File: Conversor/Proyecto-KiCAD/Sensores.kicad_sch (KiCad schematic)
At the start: 28 parts, among them U10 OPA365xxD, U7 TMCS1100A4, U8 LM5056APMH/NOPB, U9 ISO7242C

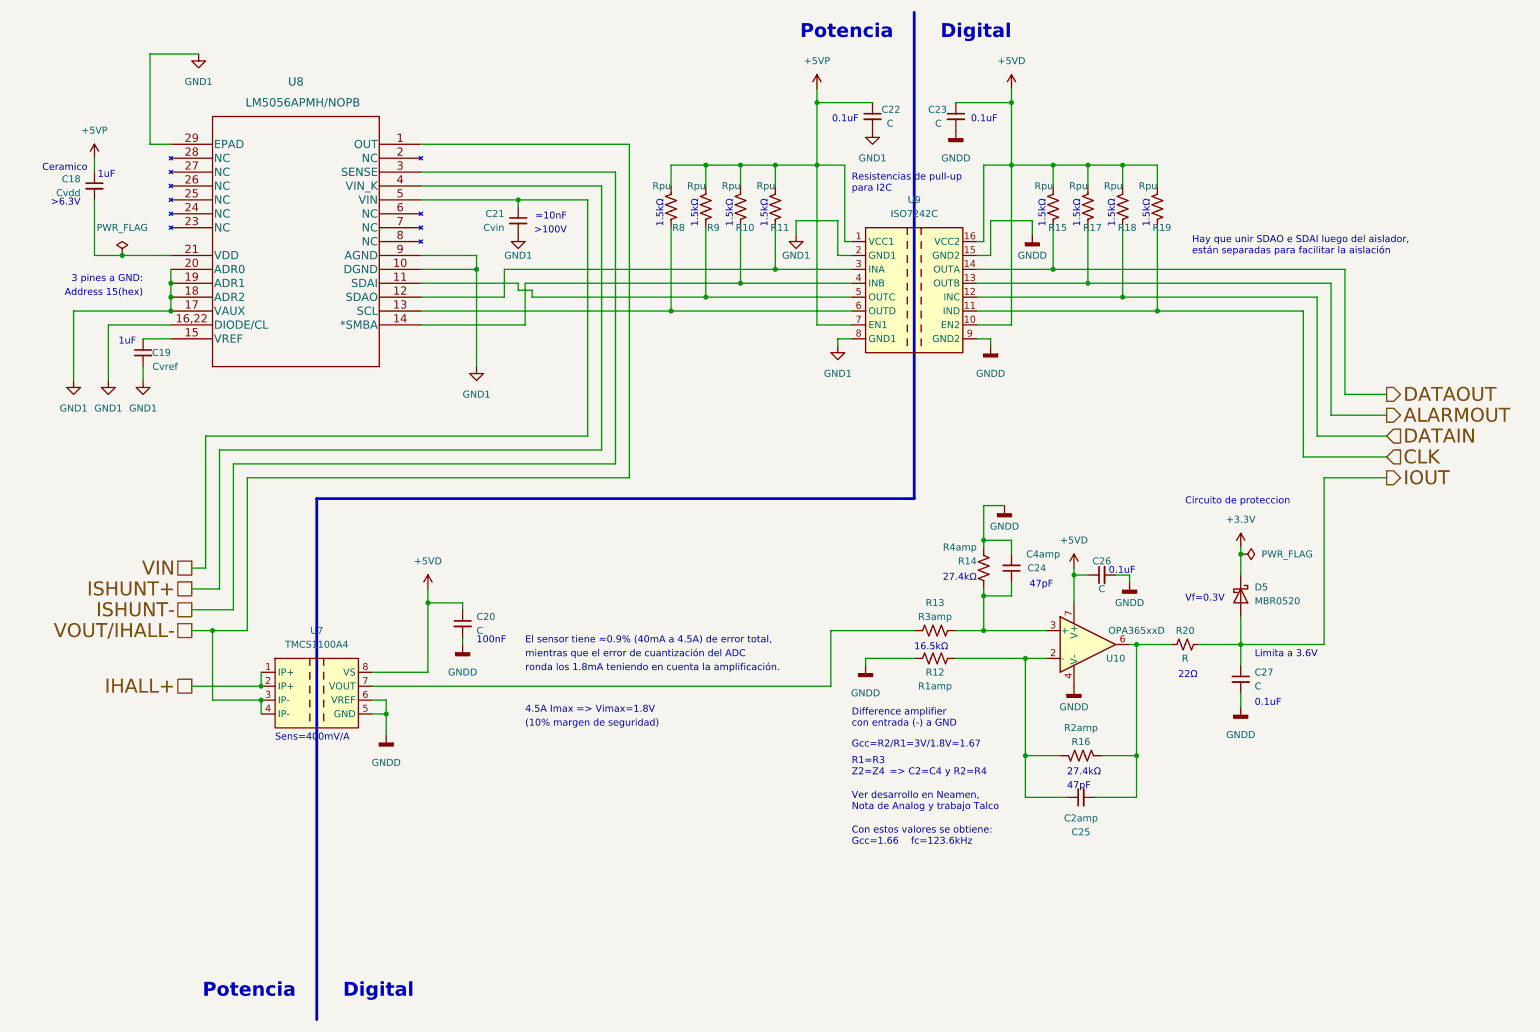
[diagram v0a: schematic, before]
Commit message: Unir las lineas de SDAI y SDAO a la salida del ISO7242C
- Espejar el esquemático en la hoja de sensores, para que sea consistente la separación de Digital/Potencia
Por hacer:

  - Verificar si es correcta la forma de conectar las lineas de datos a la salida del aislador
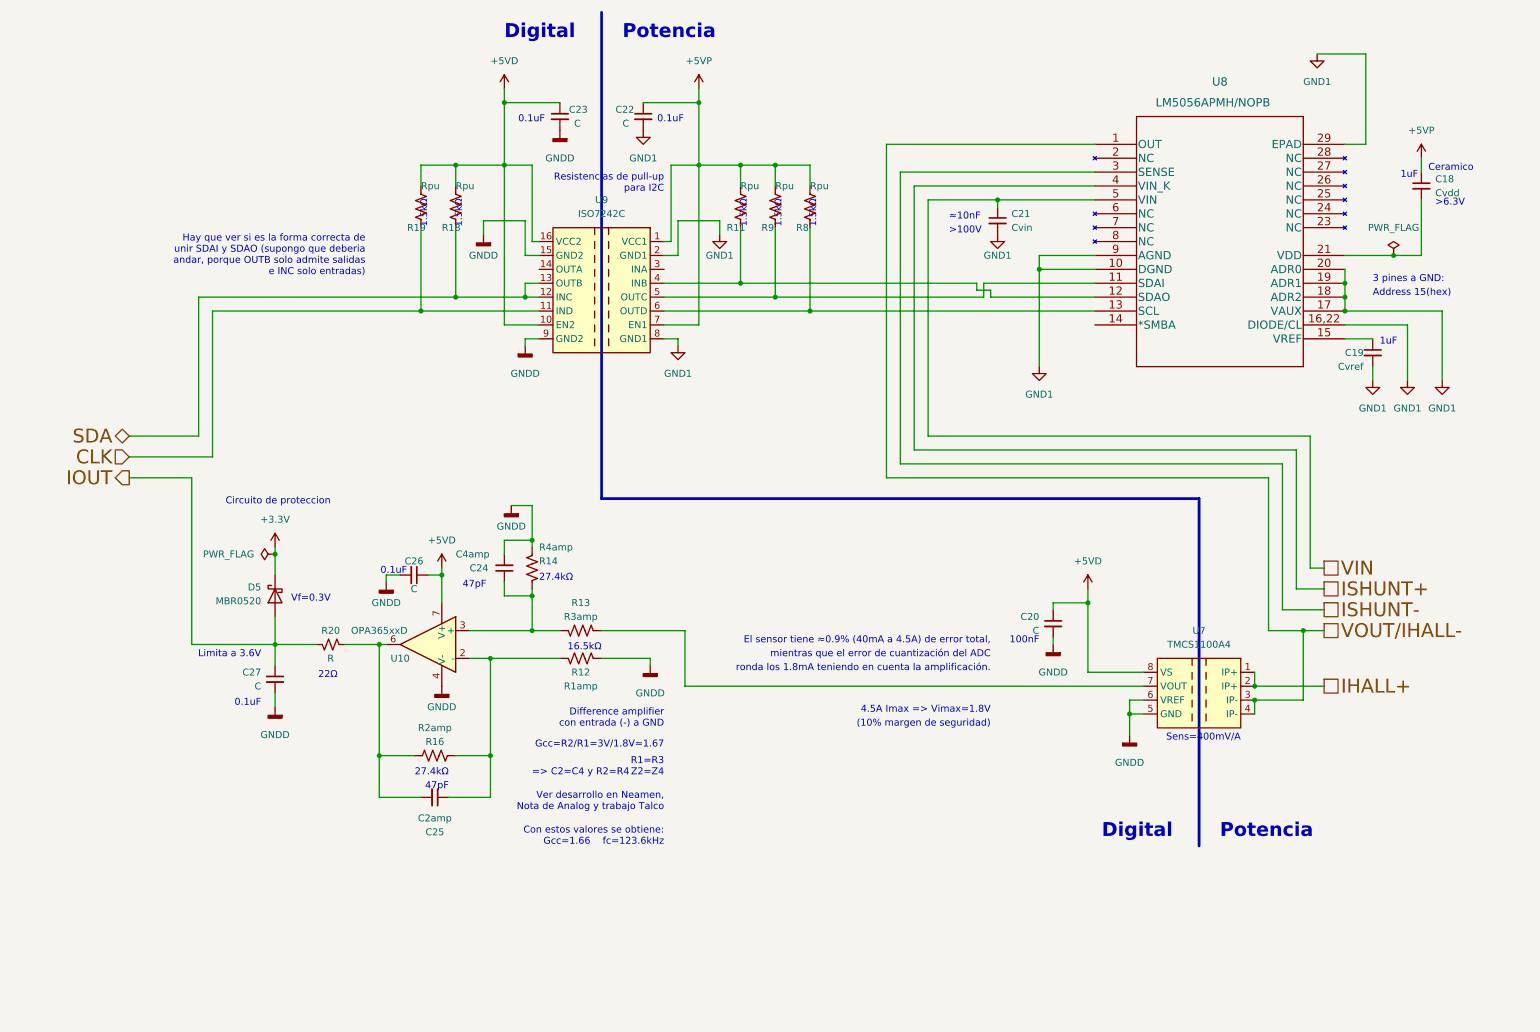
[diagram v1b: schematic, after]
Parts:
- removed R10, R15, R17: Rpu, symbol Device:R_US
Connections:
- net DATAIN is gone; now on net SDA: R18.2, U9.12 (INC)
- net at R11.2, U8.12 (SDAO): now also U9.4 (INB); no longer U9.3 (INA)
- net at U8.14 (*SMBA): no longer U9.4 (INB)
- net ALARMOUT renamed SDA
- net DATAOUT: no longer names the net of U9.14 (OUTA)
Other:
- note added: "Hay que ver si es la forma correcta de unir SDAI y SDAO (supongo que deberia andar, porque OUTB solo admite salidas e INC solo entradas)"
- note removed: "Hay que unir SDAO e SDAI luego del aislador, están separadas para facilitar la aislación"
- moved on the sheet: C18, C19, C20, C21, C22, C23, C24, C25, C26, C27, D5, R11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

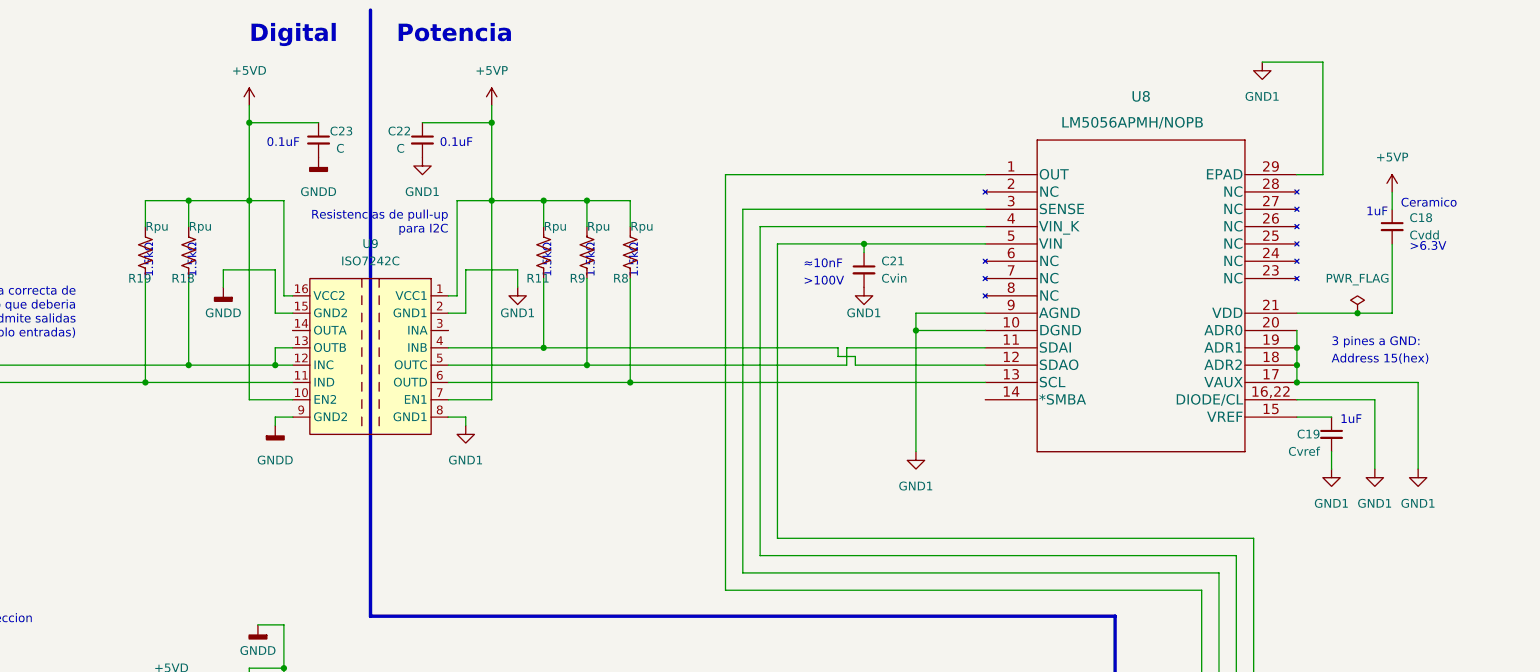
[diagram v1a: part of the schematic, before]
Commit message: Arreglar todos los errores del ERC
- Agregar flags de 'Not Connected' a pines flotantes
- Agregar resistencias 'falsas' para eliminar los errores de 'Power
input pin not connected to Power output pin'
- Agregar un GND1 conectado a PWR_FLAG para arreglar errores
- Además, agregar bien al proyecto la placa adaptadora importada a KiCad
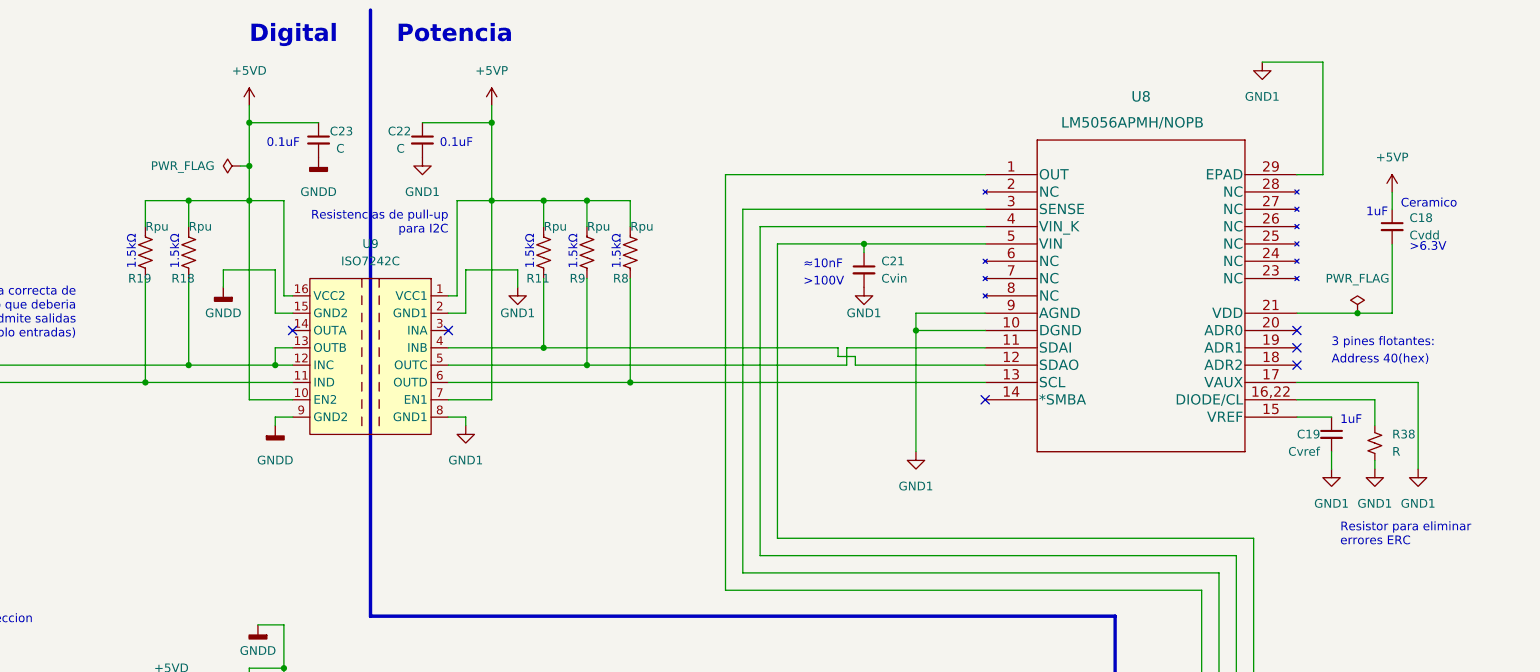
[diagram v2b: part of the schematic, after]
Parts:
- added R38: R, symbol Device:R_Small_US
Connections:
- net GND1: now also R38.2; no longer U8.16,22 (DIODE/CL), U8.18 (ADR2), U8.19 (ADR1), U8.20 (ADR0)
- new net: R38.1, U8.16,22 (DIODE/CL)
- no-connect marks 0 -> 6
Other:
- note added: "3 pines flotantes:"
- note added: "Address 40(hex)"
- note added: "Resistor para eliminar errores ERC"
- note removed: "3 pines a GND:"
- note removed: "Address 15(hex)"
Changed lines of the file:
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@@
   (junction (at 87.63 115.57) (diameter 0) (color 0 0 0 0)
   )
+  (junction (at 99.06 35.56) (diameter 0) (color 0 0 0 0)
+  )
   (junction (at 205.74 120.65) (diameter 0) (color 0 0 0 0)
   )
@@
   (junction (at 142.24 40.64) (diameter 0) (color 0 0 0 0)
   )
-  (junction (at 252.73 64.77) (diameter 0) (color 0 0 0 0)
-  )
   (junction (at 104.14 125.73) (diameter 0) (color 0 0 0 0)
   )
@@
   (junction (at 83.82 67.31) (diameter 0) (color 0 0 0 0)
   )
-  (junction (at 252.73 67.31) (diameter 0) (color 0 0 0 0)
-  )
   (junction (at 57.15 128.27) (diameter 0) (color 0 0 0 0)
   )
@@
   (junction (at 189.23 46.99) (diameter 0) (color 0 0 0 0)
   )
-  (junction (at 252.73 62.23) (diameter 0) (color 0 0 0 0)
-  )
   (junction (at 76.2 128.27) (diameter 0) (color 0 0 0 0)
   )
@@
   (junction (at 134.62 40.64) (diameter 0) (color 0 0 0 0)
   )
+  (no_connect (at 105.41 59.69))
+  (no_connect (at 128.27 59.69))
+  (no_connect (at 252.73 62.23))
+  (no_connect (at 252.73 64.77))
+  (no_connect (at 252.73 59.69))
+  (no_connect (at 207.01 69.85))
   (wire (pts (xy 132.08 135.89) (xy 132.08 125.73))
     (stroke (width 0) (type default) (color 0 0 0 0))
@@
   )
   (wire (pts (xy 96.52 156.21) (xy 88.9 156.21))
-    (stroke (width 0) (type default) (color 0 0 0 0))
-  )
-  (wire (pts (xy 252.73 59.69) (xy 252.73 62.23))
     (stroke (width 0) (type default) (color 0 0 0 0))
   )
@@
     (stroke (width 0) (type default) (color 0 0 0 0))
   )
-  (wire (pts (xy 252.73 62.23) (xy 252.73 64.77))
-    (stroke (width 0) (type default) (color 0 0 0 0))
-  )
   (wire (pts (xy 248.92 135.89) (xy 236.22 135.89))
     (stroke (width 0) (type default) (color 0 0 0 0))
@@
     (stroke (width 0) (type default) (color 0 0 0 0))
   )
-  (wire (pts (xy 196.85 59.69) (xy 196.85 77.47))
+  (wire (pts (xy 264.16 73.66) (xy 264.16 69.85))
     (stroke (width 0) (type default) (color 0 0 0 0))
   )
@@
     (stroke (width 0) (type default) (color 0 0 0 0))
   )
+  (wire (pts (xy 99.06 35.56) (xy 99.06 40.64))
+    (stroke (width 0) (type default) (color 0 0 0 0))
+  )
   (wire (pts (xy 205.74 118.11) (xy 205.74 120.65))
     (stroke (width 0) (type default) (color 0 0 0 0))
@@
     (stroke (width 0) (type default) (color 0 0 0 0))
   )
-  (wire (pts (xy 264.16 80.01) (xy 264.16 69.85))
+  (wire (pts (xy 264.16 80.01) (xy 264.16 78.74))
     (stroke (width 0) (type default) (color 0 0 0 0))
   )
@@
     (stroke (width 0) (type default) (color 0 0 0 0))
   )
-  (wire (pts (xy 99.06 29.21) (xy 99.06 40.64))
+  (wire (pts (xy 99.06 29.21) (xy 99.06 35.56))
     (stroke (width 0) (type default) (color 0 0 0 0))
   )
@@
     (stroke (width 0) (type default) (color 0 0 0 0))
   )
+  (wire (pts (xy 97.79 35.56) (xy 99.06 35.56))
+    (stroke (width 0) (type default) (color 0 0 0 0))
+  )
   (wire (pts (xy 130.81 57.15) (xy 130.81 50.8))
     (stroke (width 0) (type default) (color 0 0 0 0))
@@
     (stroke (width 0) (type default) (color 0 0 0 0))
   )
-  (wire (pts (xy 252.73 64.77) (xy 252.73 67.31))
-    (stroke (width 0) (type default) (color 0 0 0 0))
-  )
   (wire (pts (xy 215.9 140.97) (xy 213.36 140.97))
     (stroke (width 0) (type default) (color 0 0 0 0))
   )
   (wire (pts (xy 148.59 40.64) (xy 142.24 40.64))
+    (stroke (width 0) (type default) (color 0 0 0 0))
+  )
+  (wire (pts (xy 196.85 59.69) (xy 196.85 77.47))
     (stroke (width 0) (type default) (color 0 0 0 0))
   )
@@
     (effects (font (size 1.27 1.27)) (justify right bottom))
   )
-  (text "3 pines a GND:" (at 257.81 62.23 0)
-    (effects (font (size 1.27 1.27)) (justify left bottom))
-  )
-  (text "1.5kΩ" (at 143.51 52.07 90)
+  (text "3 pines flotantes:" (at 257.81 62.23 0)
+    (effects (font (size 1.27 1.27)) (justify left bottom))
+  )
+  (text "1.5kΩ" (at 140.97 50.8 90)
     (effects (font (size 1.27 1.27)) (justify left bottom))
   )
@@
     (effects (font (size 1.27 1.27)) (justify left bottom))
   )
-  (text "1.5kΩ" (at 156.21 52.07 90)
-    (effects (font (size 1.27 1.27)) (justify left bottom))
-  )
-  (text "1.5kΩ" (at 149.86 52.07 90)
-    (effects (font (size 1.27 1.27)) (justify left bottom))
-  )
-  (text "1.5kΩ" (at 91.44 52.07 90)
+  (text "1.5kΩ" (at 153.67 50.8 90)
+    (effects (font (size 1.27 1.27)) (justify left bottom))
+  )
+  (text "1.5kΩ" (at 147.32 50.8 90)
+    (effects (font (size 1.27 1.27)) (justify left bottom))
+  )
+  (text "1.5kΩ" (at 88.9 50.8 90)
     (effects (font (size 1.27 1.27)) (justify left bottom))
   )
@@
     (effects (font (size 2.54 2.54) (thickness 0.508) bold) (justify left bottom))
   )
-  (text "1.5kΩ" (at 85.09 52.07 90)
+  (text "1.5kΩ" (at 82.55 50.8 90)
+    (effects (font (size 1.27 1.27)) (justify left bottom))
+  )
+  (text "Resistor para eliminar \nerrores ERC" (at 259.08 91.44 0)
     (effects (font (size 1.27 1.27)) (justify left bottom))
   )
@@
     (effects (font (size 1.27 1.27)) (justify right bottom))
   )
-  (text "Address 15(hex)" (at 257.81 64.77 0)
+  (text "Address 40(hex)" (at 257.81 64.77 0)
     (effects (font (size 1.27 1.27)) (justify left bottom))
   )
@@
   (symbol (lib_id "power:GNDD") (at 100.33 102.87 0) (mirror y) (unit 1)
     (in_bom yes) (on_board yes)
-    (property "Reference" "#PWR?" (id 0) (at 100.33 109.22 0)
+    (property "Reference" "#PWR0101" (id 0) (at 100.33 109.22 0)
       (effects (font (size 1.27 1.27)) hide)
     )
@@
   (symbol (lib_id "power:GNDD") (at 77.47 116.84 0) (mirror y) (unit 1)
     (in_bom yes) (on_board yes)
-    (property "Reference" "#PWR?" (id 0) (at 77.47 123.19 0)
+    (property "Reference" "#PWR0104" (id 0) (at 77.47 123.19 0)
       (effects (font (size 1.27 1.27)) hide)
     )
@@
     (pin "2")
   )
+  (symbol (lib_id "power:PWR_FLAG") (at 97.79 35.56 90) (unit 1)
+    (in_bom yes) (on_board yes) (fields_autoplaced)
+    (property "Reference" "#FLG0106" (id 0) (at 95.885 35.56 0)
+      (effects (font (size 1.27 1.27)) hide)
+    )
+    (property "Value" "PWR_FLAG" (id 1) (at 93.98 35.5599 90)
+      (effects (font (size 1.27 1.27)) (justify left))
+    )
+    (property "Footprint" "" (id 2) (at 97.79 35.56 0)
+      (effects (font (size 1.27 1.27)) hide)
+    )
+    (property "Datasheet" "~" (id 3) (at 97.79 35.56 0)
+      (effects (font (size 1.27 1.27)) hide)
+    )
+    (pin "1")
+  )
   (symbol (lib_id "Device:C_Small") (at 57.15 134.62 0) (mirror y) (unit 1)
     (in_bom yes) (on_board yes) (fields_autoplaced)
@@
   (symbol (lib_id "power:+5VD") (at 87.63 114.3 0) (mirror y) (unit 1)
     (in_bom yes) (on_board yes) (fields_autoplaced)
-    (property "Reference" "#PWR?" (id 0) (at 87.63 118.11 0)
+    (property "Reference" "#PWR0105" (id 0) (at 87.63 118.11 0)
       (effects (font (size 1.27 1.27)) hide)
     )
@@
   (symbol (lib_id "power:GNDD") (at 87.63 135.89 0) (mirror y) (unit 1)
     (in_bom yes) (on_board yes)
-    (property "Reference" "#PWR?" (id 0) (at 87.63 142.24 0)
+    (property "Reference" "#PWR0102" (id 0) (at 87.63 142.24 0)
       (effects (font (size 1.27 1.27)) hide)
     )
@@
     )
     (pin "1")
+  )
+  (symbol (lib_id "Device:R_Small_US") (at 264.16 76.2 0) (unit 1)
+    (in_bom yes) (on_board yes) (fields_autoplaced)
+    (property "Reference" "R38" (id 0) (at 266.7 74.9299 0)
+      (effects (font (size 1.27 1.27)) (justify left))
+    )
+    (property "Value" "R" (id 1) (at 266.7 77.4699 0)
+      (effects (font (size 1.27 1.27)) (justify left))
+    )
+    (property "Footprint" "" (id 2) (at 264.16 76.2 0)
+      (effects (font (size 1.27 1.27)) hide)
+    )
+    (property "Datasheet" "~" (id 3) (at 264.16 76.2 0)
+      (effects (font (size 1.27 1.27)) hide)
+    )
+    (pin "1")
+    (pin "2")
   )
   (symbol (lib_id "Diode:MBR0520") (at 57.15 119.38 90) (mirror x) (unit 1)
@@
   (symbol (lib_id "power:GNDD") (at 125.73 132.08 0) (mirror y) (unit 1)
     (in_bom yes) (on_board yes) (fields_autoplaced)
-    (property "Reference" "#PWR?" (id 0) (at 125.73 138.43 0)
-      (effects (font (size 1.27 1.27)) hide)
-    )
+    (property "Reference" "#PWR0103" (id 0) (at 125.73 138.43 0)
+      (effects (font (size 1.27 1.27)) hide)
+    )
